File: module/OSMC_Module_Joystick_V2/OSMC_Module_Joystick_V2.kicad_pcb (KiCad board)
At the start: 4 copper layers, 34 x 41 mm, 6 parts, among them U1 OSMC Module Board w/pins, U2 24LC02BT-I/OT, U3 ADS1115IDGS, U4 COM-09032

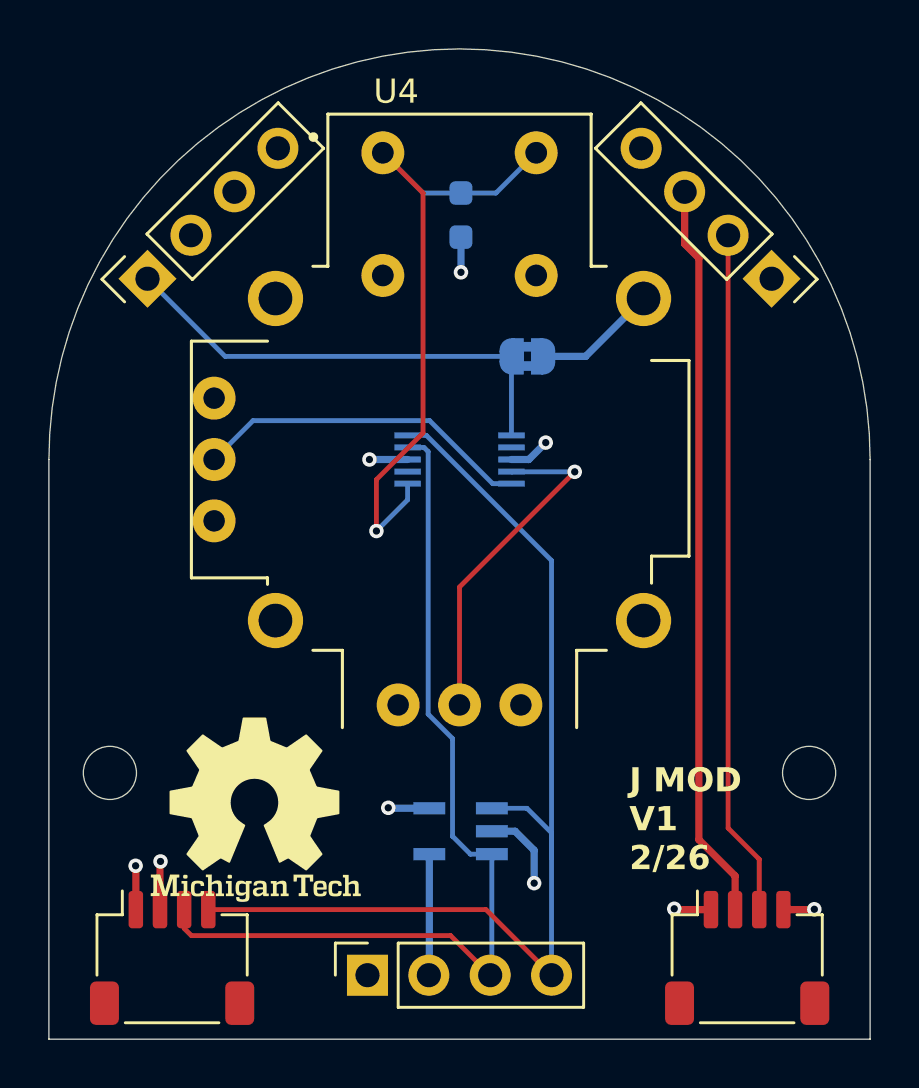
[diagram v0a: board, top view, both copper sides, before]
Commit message: more hand solderable joystick
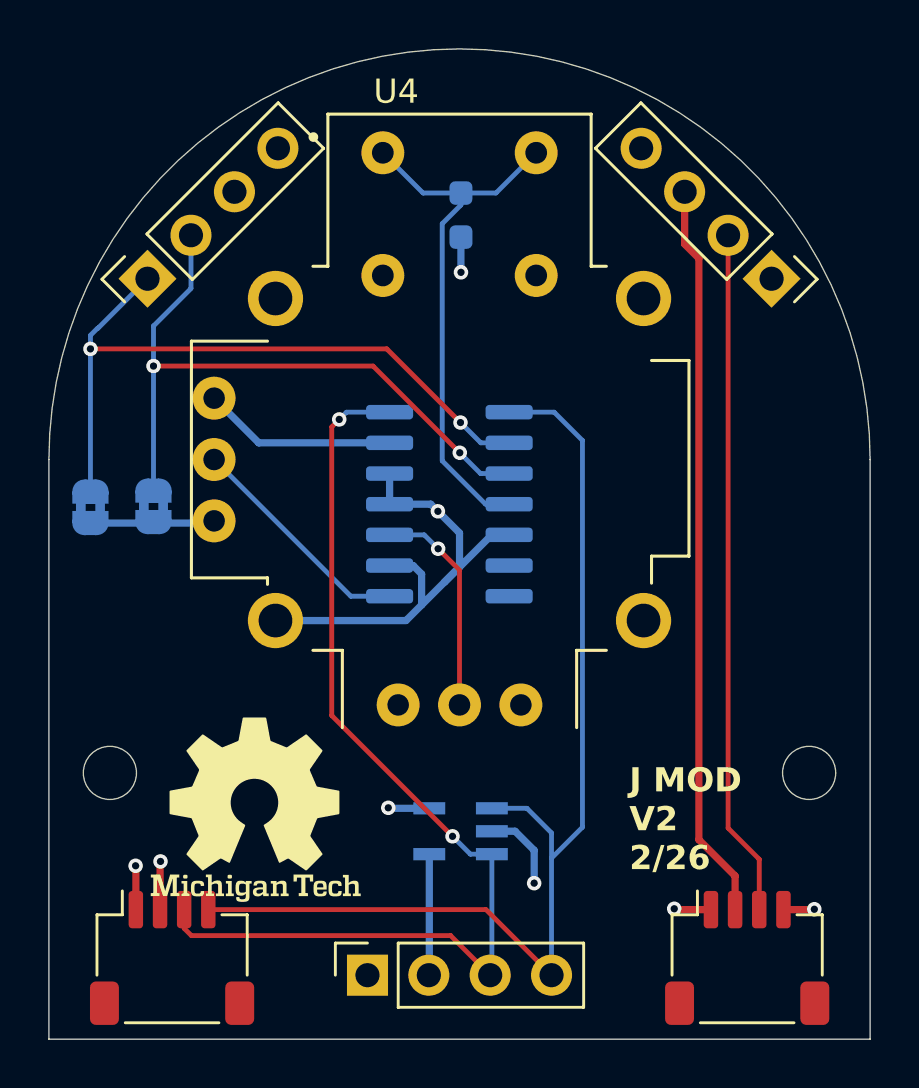
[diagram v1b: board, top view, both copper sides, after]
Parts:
- removed U3: ADS1115IDGS, Library:TSSOP-10_3x3mm_P0.5mm
- added JP2: SolderJumper_2_Bridged, Jumper:SolderJumper-2_P1.3mm_Bridged2Bar_RoundedPad1.0x1.5mm, B.Cu at (181.8, 77.7)
- added U5: MCP3428x-xSL, Package_SO:SOIC-14_3.9x8.7mm_P1.27mm, B.Cu at (196.6, 77.6)
- moved JP1 16.7 mm to (184.4, 77.7), turned to 90 degrees
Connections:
- U1 pad 19: unconnected-(U1-A2-Pad19) -> /A1
- U1 pad 20: /A1 -> /A0
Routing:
- net /A0: track 0.00 -> 28.7 mm, vias 0 -> 2
- net GND: track 15.4 -> 34.5 mm
- net /A1: track 19.7 -> 27.8 mm, vias 0 -> 2
- net /3v3: track 11.3 -> 17.8 mm, vias 4 -> 3
- net Net-(U4-H): track 14.2 -> 9.08 mm
- net Net-(U5-CH3+): track 27.4 -> 22.7 mm, vias 1 -> 0
- net Net-(U4-V): track 14.1 -> 9.61 mm
- net /SDA: track 38.5 -> 42.9 mm, vias 0 -> 2
- net /SCL: track 44.5 -> 45.5 mm
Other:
- board text added: "J MOD V2 2/26"
- board text removed: "J MOD V1 2/26"

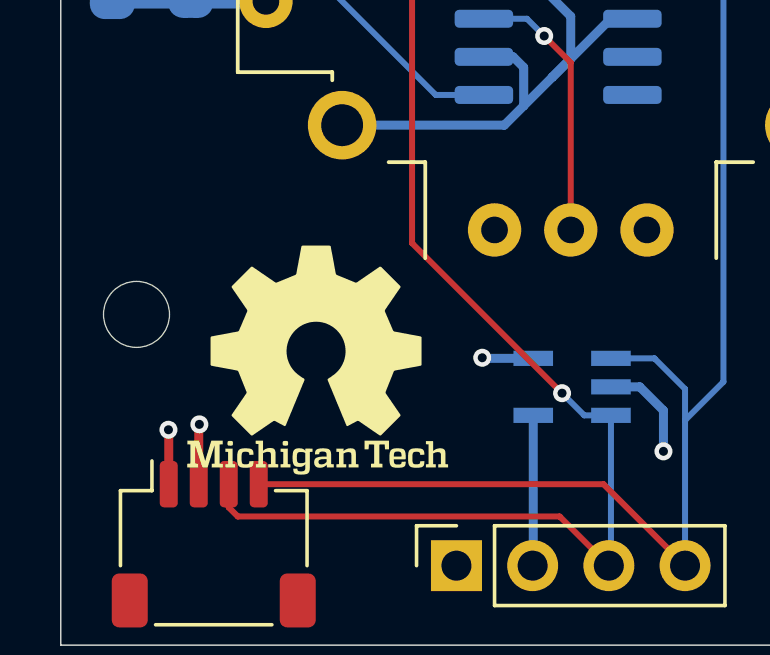
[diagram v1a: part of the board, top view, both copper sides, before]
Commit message: update to pcb, fixed i2c lines for bus 0 and 1
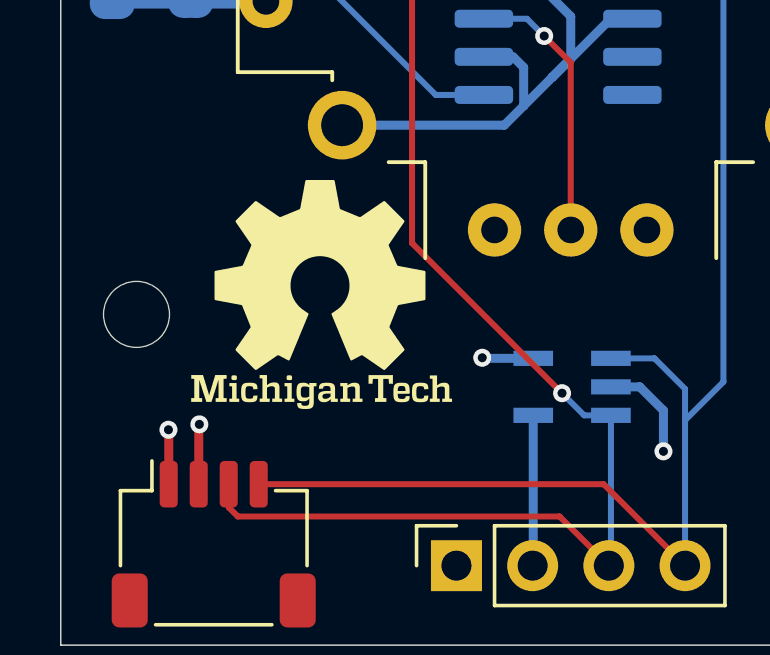
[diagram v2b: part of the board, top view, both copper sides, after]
